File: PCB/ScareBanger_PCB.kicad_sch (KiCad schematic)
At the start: 15 parts, among them J1 RJ45, J16 Conn_01x10_Female - SAINSMART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, J17 Screw_Terminal_01x10 - HILETG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, J2 1757271, J3 Screw_Terminal_01x06, J4 Barrel_Jack_Switch, J6 Screw_Terminal_01x06, J7 Screw_Terminal_01x06, SW1 SW_SPDT, SW2 SW_SPDT

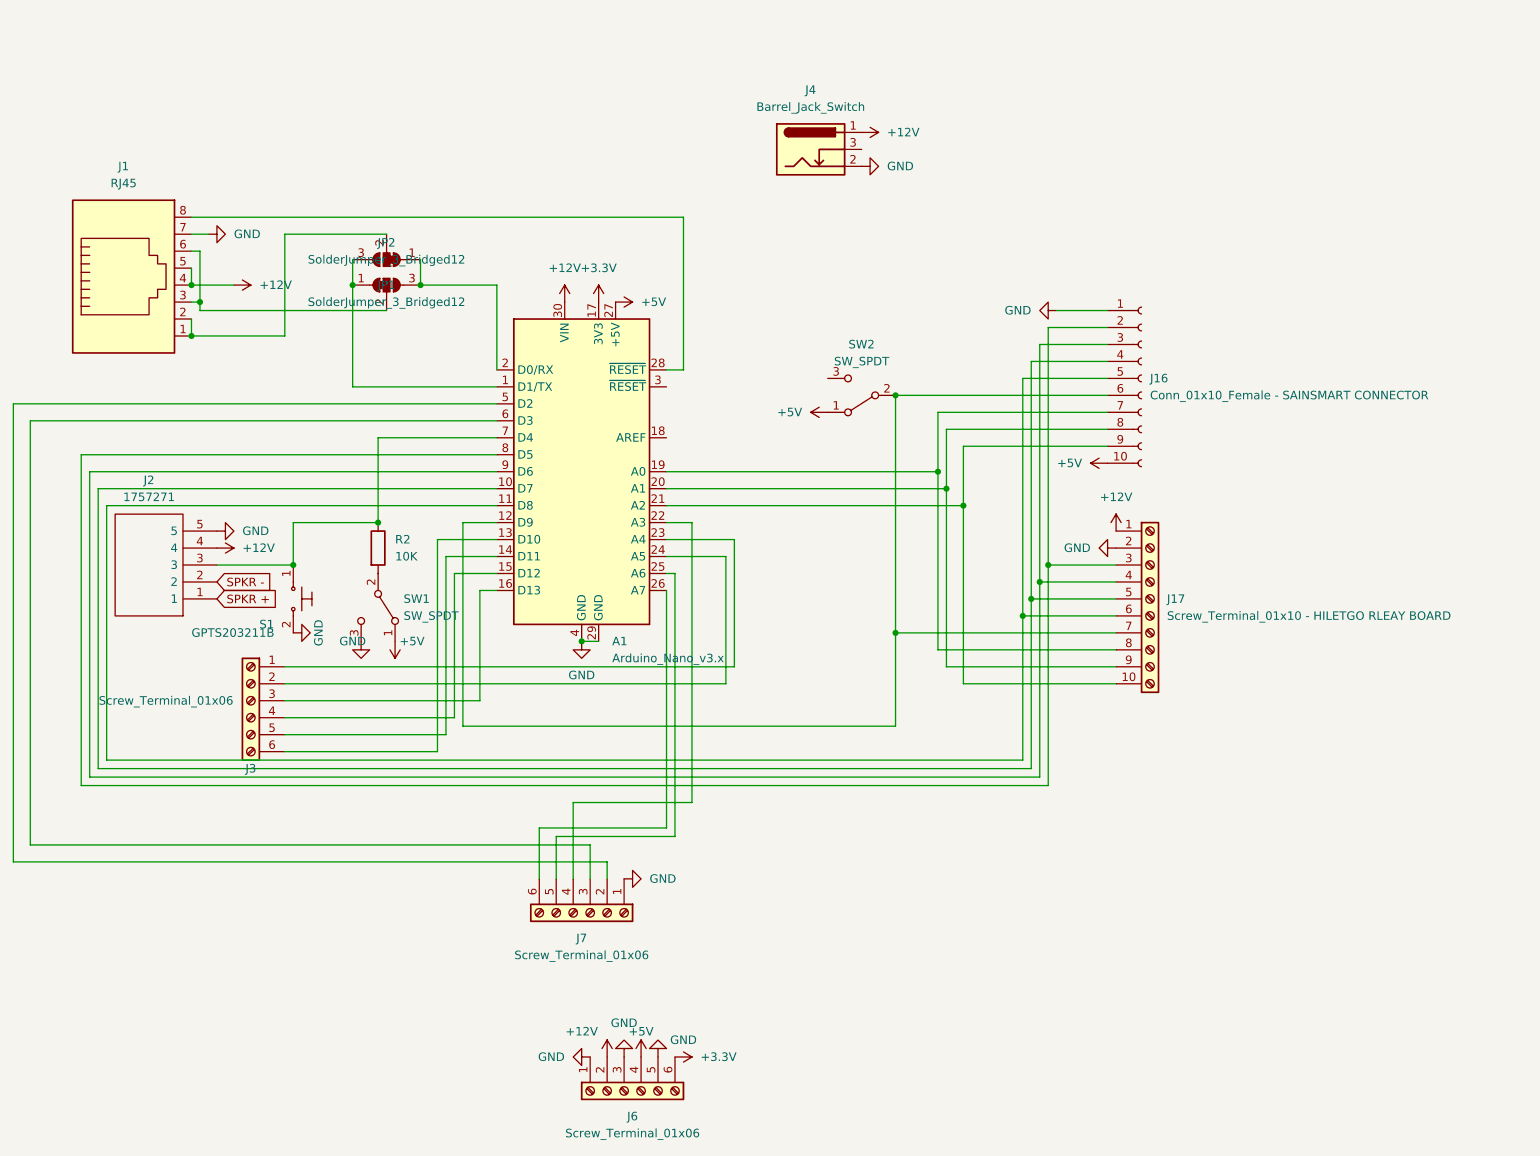
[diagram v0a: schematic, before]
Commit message: add mp3 module
added mp3 module, both dfplayer and yx5300 options, re-did layout for the mp3 player and the headphone jack options.
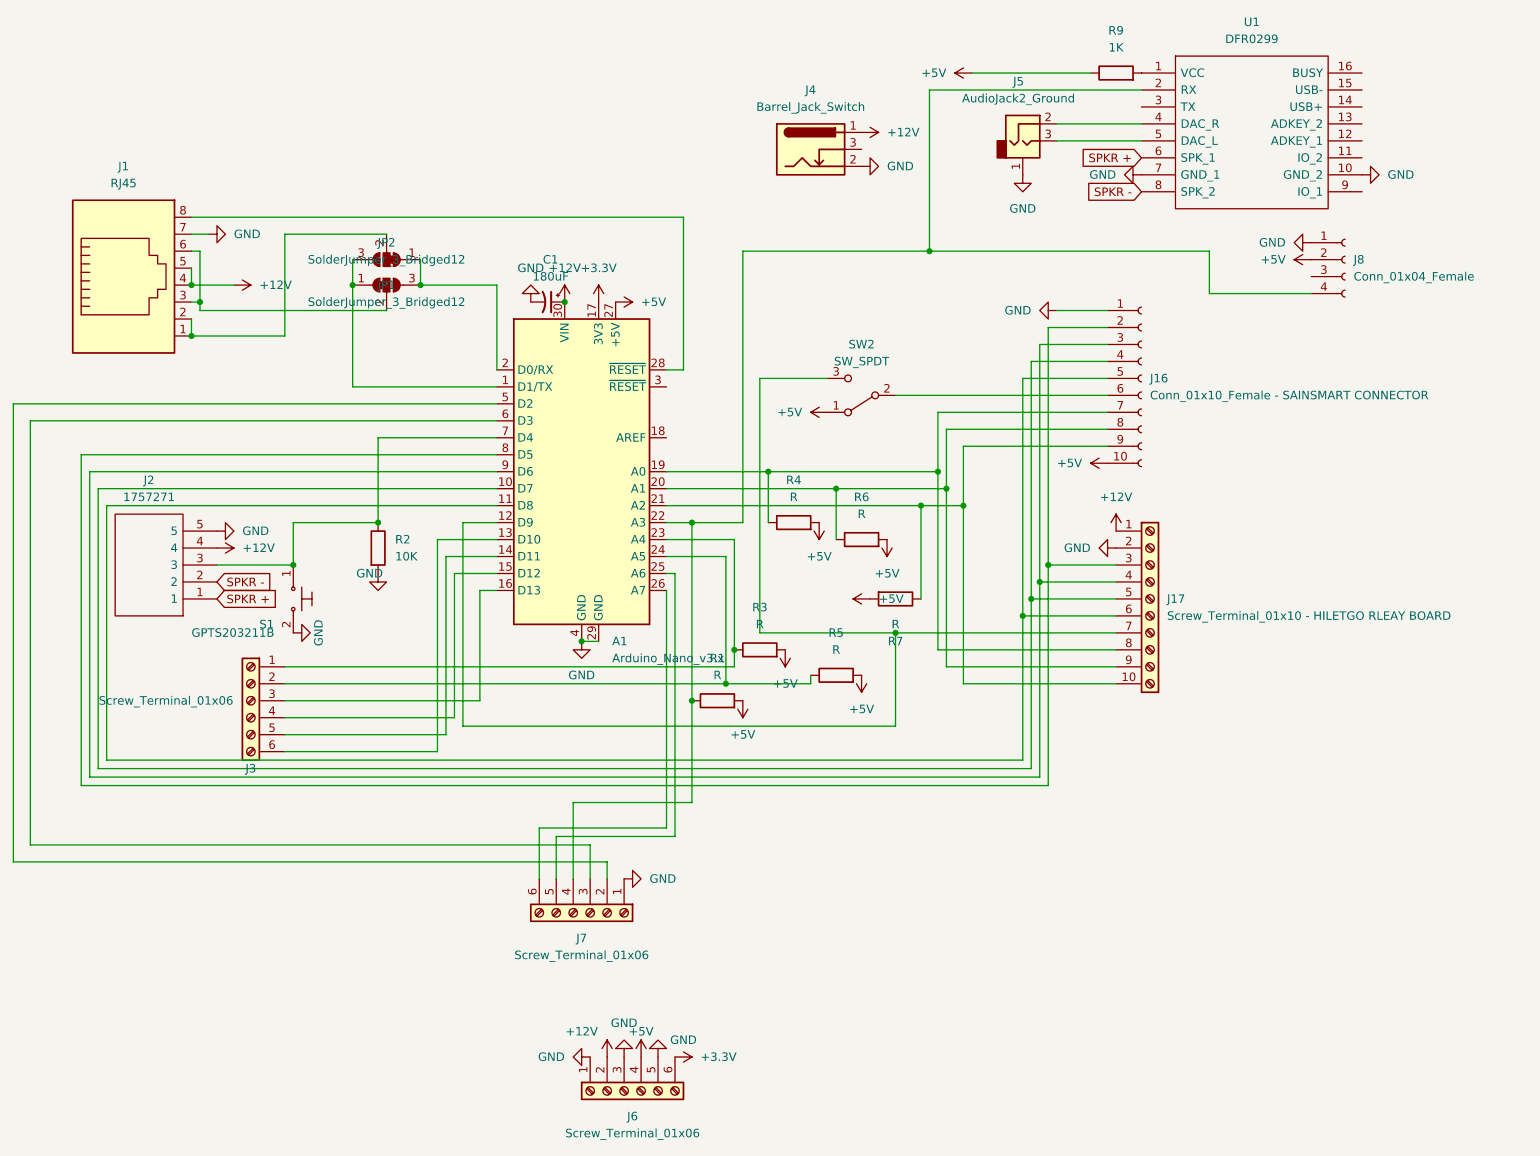
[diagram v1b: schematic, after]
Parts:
- removed SW1: SW_SPDT, custom:SpDt SlideSwitch, symbol Switch:SW_SPDT
- added C1: 180uF, Capacitor_THT:CP_Radial_D6.3mm_P2.50mm, symbol Device:C_Polarized_Small_US
- added J5: AudioJack2_Ground, custom:PJ-301C HeadPhoneJack, symbol Connector:AudioJack2_Ground
- added J8: Conn_01x04_Female, Connector_PinHeader_2.54mm:PinHeader_1x04_P2.54mm_Vertical, symbol Connector:Conn_01x04_Female
- added R1, R3, R4, R5, R6, R7: R, Resistor_THT:R_Axial_DIN0207_L6.3mm_D2.5mm_P2.54mm_Vertical, symbol Device:R
- added R9: 1K, Resistor_THT:R_Axial_DIN0207_L6.3mm_D2.5mm_P7.62mm_Horizontal, symbol Device:R
- added U1: DFR0299, SamacSys_Parts:DIPS1778W50P254L2100H170Q16N, symbol SamacSys_Parts:DFR0299
- R2: footprint Resistor_THT:R_Axial_DIN0516_L15.5mm_D5.0mm_P5.08mm_Vertical -> Resistor_THT:R_Axial_DIN0207_L6.3mm_D2.5mm_P2.54mm_Vertical
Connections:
- net +12V: now also C1.1
- net +5V: now also J8.2 (Pin_2), R1.2, R3.2, R4.2, R5.2, R6.2, R7.2, R9.1
- net GND: now also R2.2, C1.2, J5.1, J8.1 (Pin_1), U1.10 (GND_2), U1.7 (GND_1)
- net SPKR +: now also U1.6 (SPK_1)
- net SPKR -: now also U1.8 (SPK_2)
- net at J16.6 (Pin_6), SW2.2 (B): no longer A1.12 (D9), J17.7 (Pin_7)
- net at A1.19 (A0), J16.7 (Pin_7), J17.8 (Pin_8): now also R4.1
- net at A1.20 (A1), J16.8 (Pin_8), J17.9 (Pin_9): now also R6.1
- net at A1.21 (A2), J16.9 (Pin_9), J17.10 (Pin_10): now also R7.1
- net at SW2.3 (C): now also A1.12 (D9), J17.7 (Pin_7)
- net at A1.22 (A3), J7.4 (Pin_4): now also J8.4 (Pin_4), R1.1, U1.2 (RX)
- net at A1.23 (A4), J3.1 (Pin_1): now also R3.1
- net at A1.24 (A5), J3.2 (Pin_2): now also R5.1
- new net: J5.2, U1.4 (DAC_R)
- new net: J5.3, U1.5 (DAC_L)
- new net: R9.2, U1.1 (VCC)
